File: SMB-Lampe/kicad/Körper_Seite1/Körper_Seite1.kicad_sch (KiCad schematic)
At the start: 24 parts, among them J10 Conn_01x01_Pin, J11 Conn_01x01_Pin, J12 Conn_01x01_Pin, J7 Conn_01x01_Pin, J8 Conn_01x01_Pin, J9 Conn_01x01_Pin

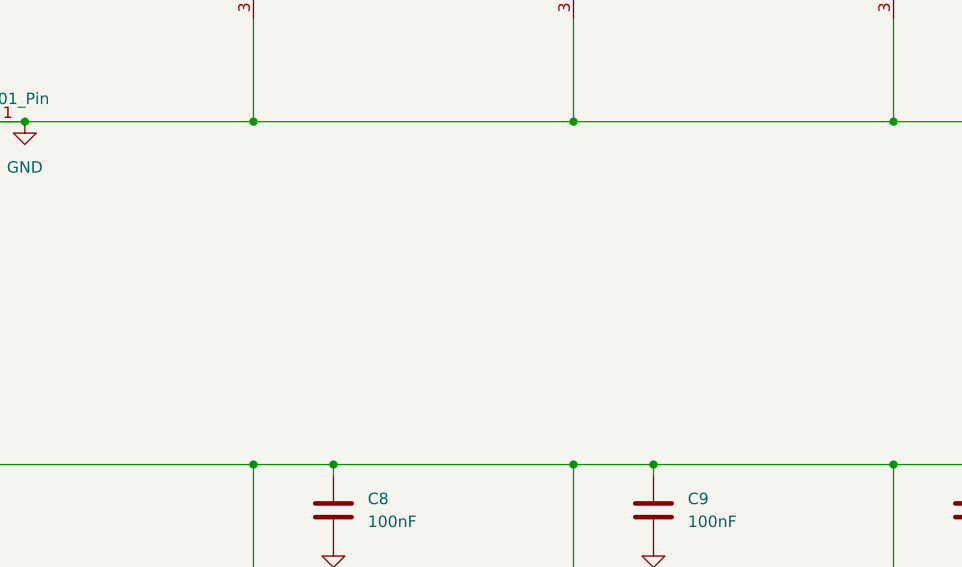
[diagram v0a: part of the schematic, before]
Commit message: Alle Platinen erstellt
Alle Platinen wurden im Projekt einzeln erstellt.
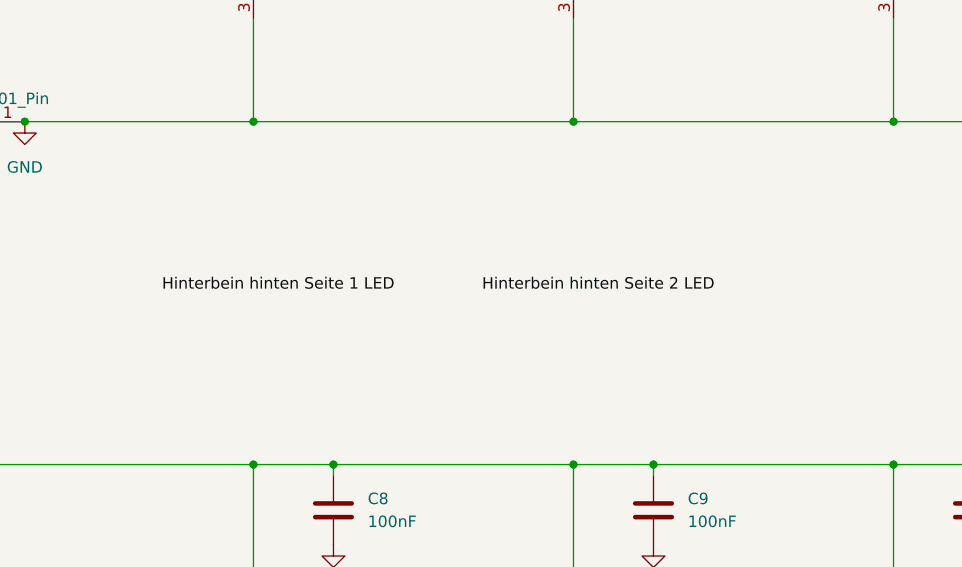
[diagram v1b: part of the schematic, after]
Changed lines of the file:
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@@
+		)
+	)
+	(label "Hinterbein hinten Seite 2 LED"
+		(at 88.9 82.55 0)
+		(effects
+			(font
+				(size 1.27 1.27)
+			)
+			(justify left bottom)
+		)
+	)
+	(label "Hinterbein hinten Seite 1 LED"
+		(at 53.34 82.55 0)
+		(effects
+			(font
+				(size 1.27 1.27)
+			)
+			(justify left bottom)
 		)
 	)

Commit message: Alle LEDs nochmal richtig angeschlossen
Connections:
- net Data: now also D7.2 (DOUT), D8.4 (DIN); no longer D7.4 (DIN), D8.2 (DOUT)
- net Data_In: now also D3.4 (DIN); no longer D3.2 (DOUT)
- net Data_OUT: now also D11.2 (DOUT); no longer D11.4 (DIN)
- net GND: no longer C10.1, C11.1, C3.1, C4.1, C5.1, C6.1, C7.1, C8.1, C9.1, D10.1 (VDD), D11.1 (VDD), D3.1 (VDD), D4.1 (VDD), D5.1 (VDD), D6.1 (VDD), D7.1 (VDD), D8.1 (VDD), D9.1 (VDD), J10.1 (Pin_1), J7.1 (Pin_1)
- net at D9.2 (DOUT): now also D10.4 (DIN); no longer D8.4 (DIN)
- net at D9.4 (DIN): now also D8.2 (DOUT); no longer D10.2 (DOUT)
- net at D6.2 (DOUT): now also D7.4 (DIN); no longer D5.4 (DIN)
- net at D6.4 (DIN): now also D5.2 (DOUT); no longer D7.2 (DOUT)
- net at D4.2 (DOUT): now also D5.4 (DIN); no longer D3.4 (DIN)
- net at D4.4 (DIN): now also D3.2 (DOUT); no longer D5.2 (DOUT)
- new net: D10.2 (DOUT), D11.4 (DIN)
- new net +5V: C10.1, C11.1, C3.1, C4.1, C5.1, C6.1, C7.1, C8.1, C9.1, D10.1 (VDD), D11.1 (VDD), D3.1 (VDD), D4.1 (VDD), D5.1 (VDD), D6.1 (VDD), D7.1 (VDD), D8.1 (VDD), D9.1 (VDD), J10.1 (Pin_1), J7.1 (Pin_1)
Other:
- moved on the sheet: C10, C11, C3, C4, C5, C6, C7, C8, C9

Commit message: Hinterbein Seite 1/2 erstellt
Anschlüsse zwischen den Platinen mit MountingHoles. Eigenes MountingHole Erstellt
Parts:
- J10, J11, J12, J7, J8, J9: footprint TestPoint:TestPoint_Pad_1.0x1.0mm -> TestPoint:TestPoint_Pad_2.0x2.0mm
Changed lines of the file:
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@@
 			)
 		)
-		(property "Footprint" "TestPoint:TestPoint_Pad_1.0x1.0mm"
+		(property "Footprint" "TestPoint:TestPoint_Pad_2.0x2.0mm"
 			(at 33.02 44.45 0)
 			(effects
@@
 			)
 		)
-		(property "Footprint" "TestPoint:TestPoint_Pad_1.0x1.0mm"
+		(property "Footprint" "TestPoint:TestPoint_Pad_2.0x2.0mm"
 			(at 33.02 25.4 0)
 			(effects
@@
 			)
 		)
-		(property "Footprint" "TestPoint:TestPoint_Pad_1.0x1.0mm"
+		(property "Footprint" "TestPoint:TestPoint_Pad_2.0x2.0mm"
 			(at 33.02 63.5 0)
 			(effects
@@
 			)
 		)
-		(property "Footprint" "TestPoint:TestPoint_Pad_1.0x1.0mm"
+		(property "Footprint" "TestPoint:TestPoint_Pad_2.0x2.0mm"
 			(at 259.08 101.6 0)
 			(effects
@@
 			)
 		)
-		(property "Footprint" "TestPoint:TestPoint_Pad_1.0x1.0mm"
+		(property "Footprint" "TestPoint:TestPoint_Pad_2.0x2.0mm"
 			(at 259.08 139.7 0)
 			(effects
@@
 			)
 		)
-		(property "Footprint" "TestPoint:TestPoint_Pad_1.0x1.0mm"
+		(property "Footprint" "TestPoint:TestPoint_Pad_2.0x2.0mm"
 			(at 259.08 120.65 0)
 			(effects

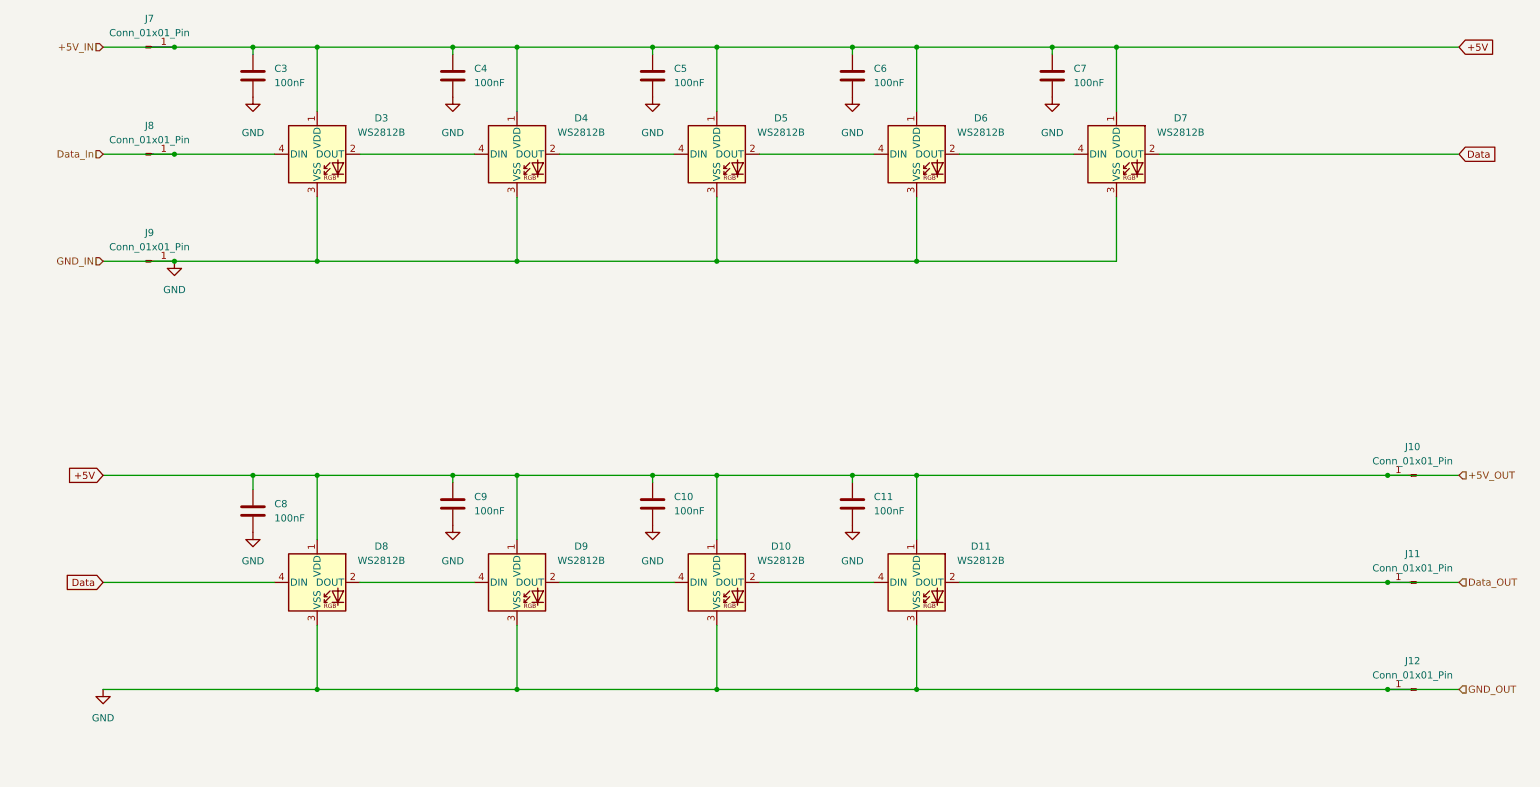
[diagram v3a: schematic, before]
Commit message: Vorderseite Platine Körper Seite 1 fertig
zwei GND Verbindungen fehlen noch
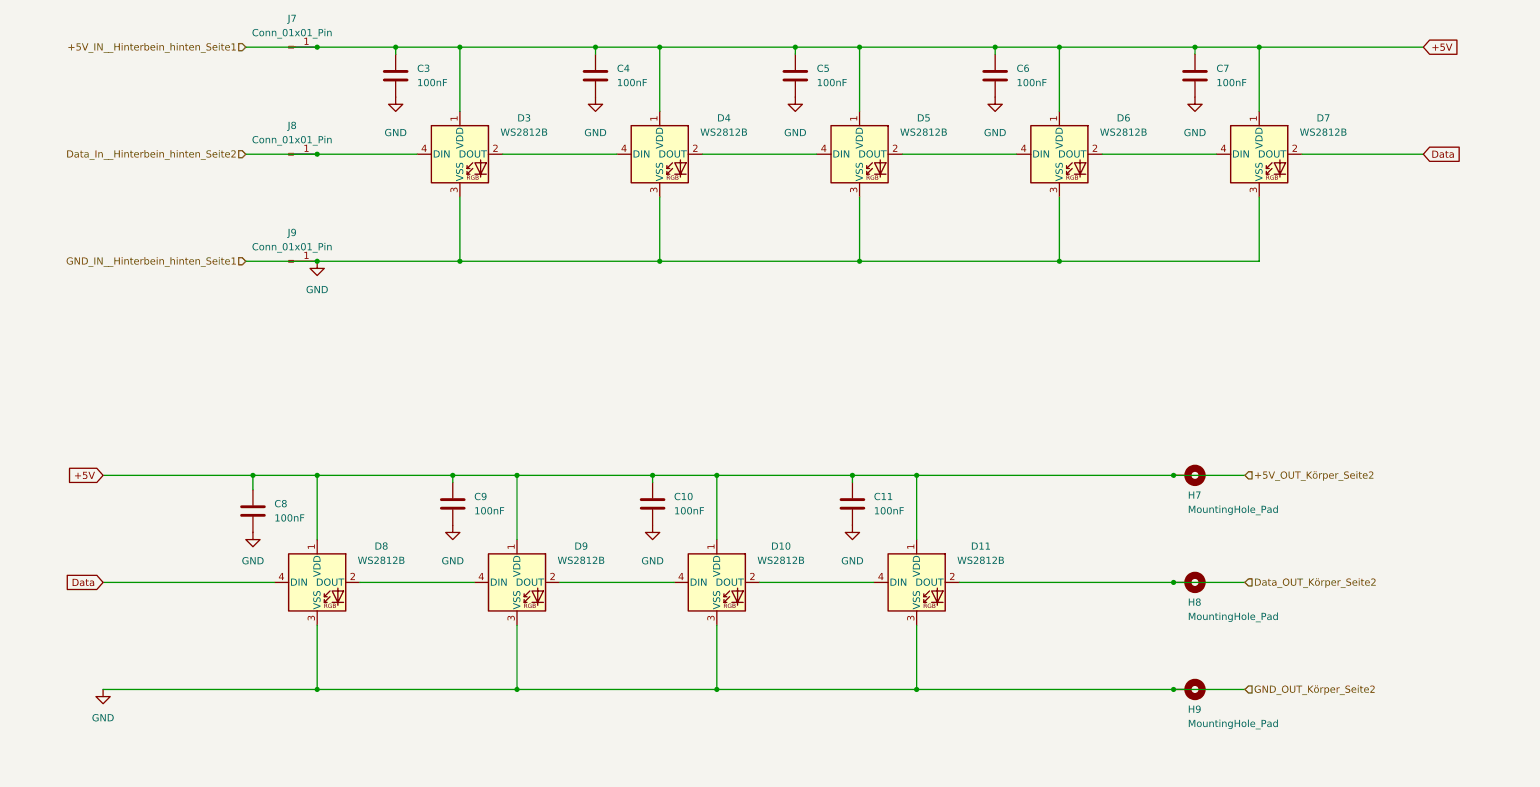
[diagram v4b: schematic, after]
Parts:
- removed J10, J11, J12: Conn_01x01_Pin, TestPoint:TestPoint_Pad_2.0x2.0mm, symbol Connector:Conn_01x01_Pin
- added H7, H8, H9: MountingHole_Pad, Eigenen_Library:MountingHole D2 x d1 test, symbol Mechanical:MountingHole_Pad
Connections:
- net +5V: now also H7.1
- net GND: now also H9.1
- net Data_In renamed Data_In__Hinterbein_hinten_Seite2
- net Data_OUT renamed Data_OUT_Körper_Seite2
- net Data_OUT_Körper_Seite2: now also H8.1
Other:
- moved on the sheet: C3, C4, C5, C6, C7, D3, D4, D5, D6, D7, J7, J8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

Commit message: Körper mit Vorder und Rückseite fertig
Alle Leiterbahnen sind gelegt und Verbindungen zu den anderen Platinen platziert
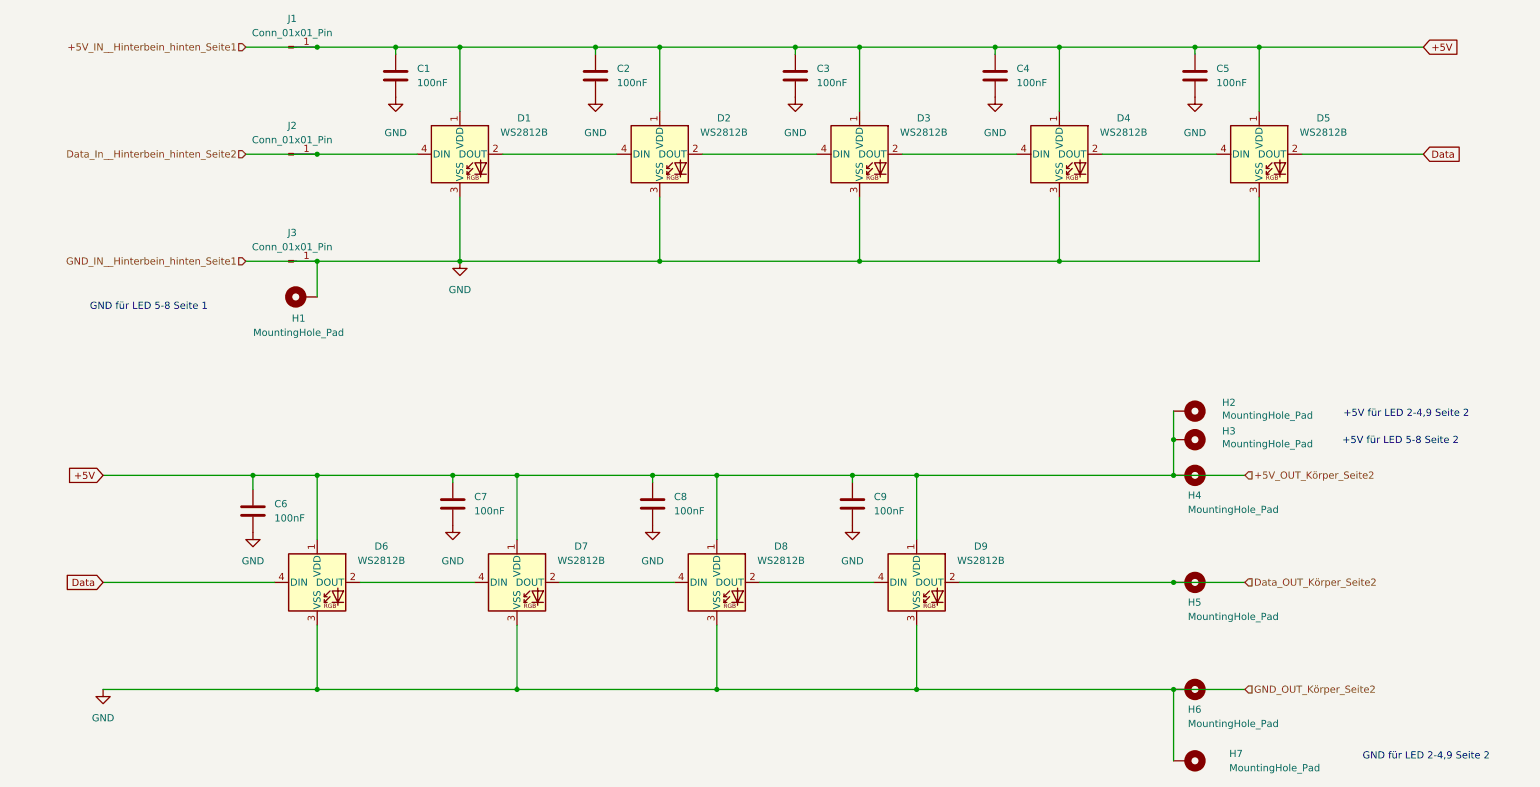
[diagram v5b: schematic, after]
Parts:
- added H1, H2, H3, H7: MountingHole_Pad, Eigenen_Library:MountingHole D2 x d1 test, symbol Mechanical:MountingHole_Pad
- renumbered C3 to C1, C4 to C2, C5 to C3, C6 to C4, C7 to C5, C8 to C6, C9 to C7, C10 to C8, C11 to C9, D3 to D1, D4 to D2, D5 to D3, D6 to D4, D7 to D5, D8 to D6, D9 to D7, D10 to D8, D11 to D9, H7 to H4, H8 to H5, H9 to H6, J7 to J1, J8 to J2, J9 to J3
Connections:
- net +5V: now also H2.1, H3.1
- net GND: now also H1.1, H7.1
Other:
- note added: "+5V für LED 2-4,9 Seite 2"
- note added: "+5V für LED 5-8 Seite 2"
- note added: "GND für LED 2-4,9 Seite 2"
- note added: "GND für LED 5-8 Seite 1"

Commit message: Vorderes Hinterbein fertig
Alle Platinen sind fertig beschaltet
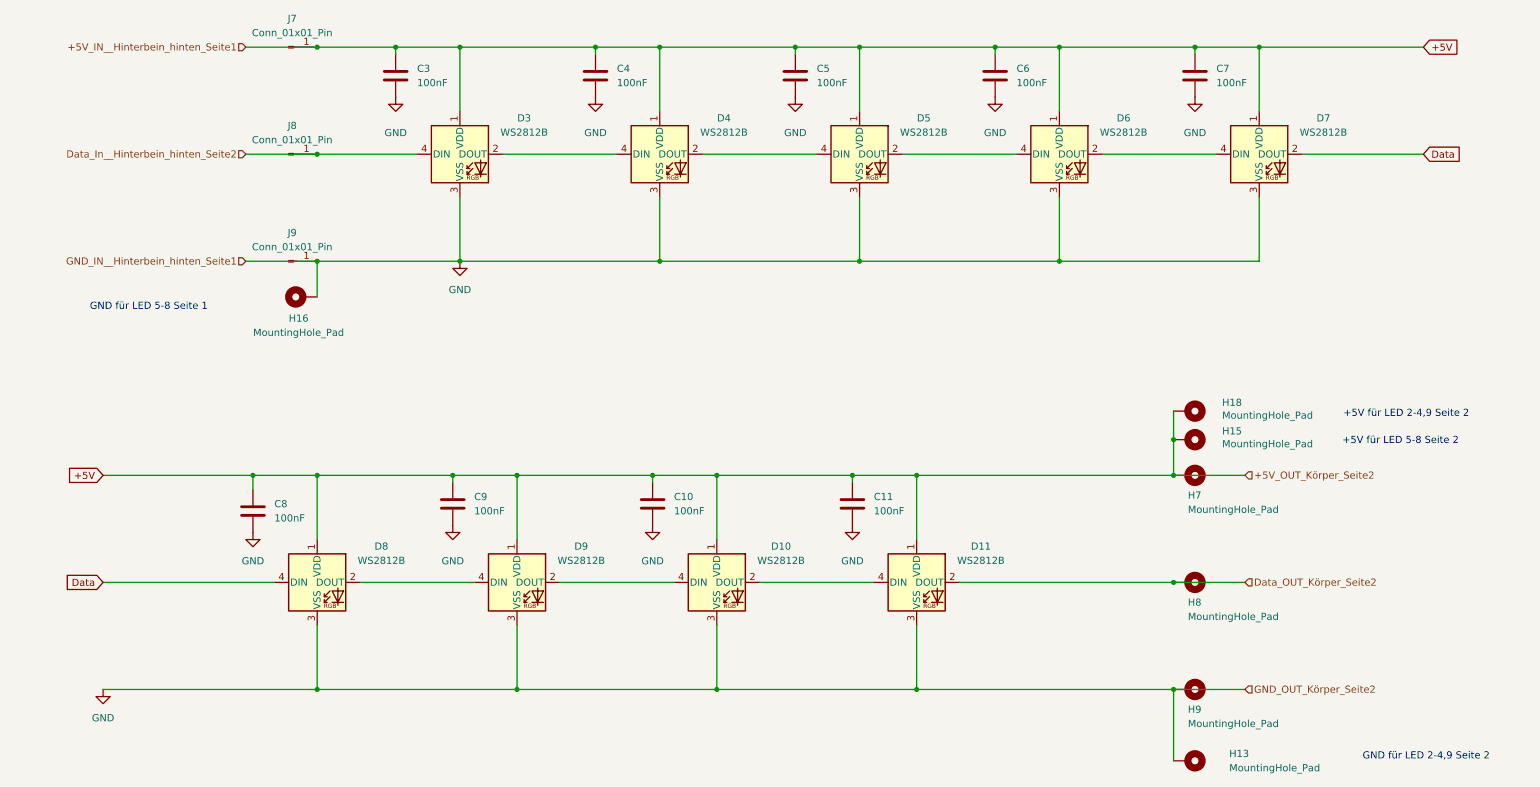
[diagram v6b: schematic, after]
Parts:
- renumbered C8 to C10, C9 to C11, C1 to C3, C2 to C4, C3 to C5, C4 to C6, C5 to C7, C6 to C8, C7 to C9, D8 to D10, D9 to D11, D1 to D3, D2 to D4, D3 to D5, D4 to D6, D5 to D7, D6 to D8, D7 to D9, H7 to H13, H3 to H15, H1 to H16, H2 to H18, H4 to H7, H5 to H8, H6 to H9, J1 to J7, J2 to J8, J3 to J9

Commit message: Hinterbeine Geändert teilweiße Körper
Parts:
- C10, C11, C3, C4, C5, C6, C7, C8, C9: footprint Capacitor_SMD:C_0201_0603Metric -> Capacitor_SMD:C_0603_1608Metric_Pad1.08x0.95mm_HandSolder
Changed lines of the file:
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@@
 			)
 		)
-		(property "Footprint" "Capacitor_SMD:C_0201_0603Metric"
+		(property "Footprint" "Capacitor_SMD:C_0603_1608Metric_Pad1.08x0.95mm_HandSolder"
 			(at 159.7152 110.49 0)
 			(effects
@@
 			)
 		)
-		(property "Footprint" "Capacitor_SMD:C_0201_0603Metric"
+		(property "Footprint" "Capacitor_SMD:C_0603_1608Metric_Pad1.08x0.95mm_HandSolder"
 			(at 78.4352 34.29 0)
 			(effects
@@
 			)
 		)
-		(property "Footprint" "Capacitor_SMD:C_0201_0603Metric"
+		(property "Footprint" "Capacitor_SMD:C_0603_1608Metric_Pad1.08x0.95mm_HandSolder"
 			(at 149.5552 34.29 0)
 			(effects
@@
 			)
 		)
-		(property "Footprint" "Capacitor_SMD:C_0201_0603Metric"
+		(property "Footprint" "Capacitor_SMD:C_0603_1608Metric_Pad1.08x0.95mm_HandSolder"
 			(at 220.6752 34.29 0)
 			(effects
@@
 			)
 		)
-		(property "Footprint" "Capacitor_SMD:C_0201_0603Metric"
+		(property "Footprint" "Capacitor_SMD:C_0603_1608Metric_Pad1.08x0.95mm_HandSolder"
 			(at 88.5952 110.49 0)
 			(effects
@@
 			)
 		)
-		(property "Footprint" "Capacitor_SMD:C_0201_0603Metric"
+		(property "Footprint" "Capacitor_SMD:C_0603_1608Metric_Pad1.08x0.95mm_HandSolder"
 			(at 53.0352 111.76 0)
 			(effects
@@
 			)
 		)
-		(property "Footprint" "Capacitor_SMD:C_0201_0603Metric"
+		(property "Footprint" "Capacitor_SMD:C_0603_1608Metric_Pad1.08x0.95mm_HandSolder"
 			(at 185.1152 34.29 0)
 			(effects
@@
 			)
 		)
-		(property "Footprint" "Capacitor_SMD:C_0201_0603Metric"
+		(property "Footprint" "Capacitor_SMD:C_0603_1608Metric_Pad1.08x0.95mm_HandSolder"
 			(at 113.9952 34.29 0)
 			(effects
@@
 			)
 		)
-		(property "Footprint" "Capacitor_SMD:C_0201_0603Metric"
+		(property "Footprint" "Capacitor_SMD:C_0603_1608Metric_Pad1.08x0.95mm_HandSolder"
 			(at 124.1552 110.49 0)
 			(effects

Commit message: Nachträgliche Änderungen für die Fertigung und Präsentation
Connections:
- net +5V renamed +5V_1
- net Data renamed Data1
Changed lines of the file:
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@@
 		)
 	)
-	(global_label "Data"
+	(global_label "Data1"
 		(shape input)
 		(at 25.4 120.65 180)
@@
 		)
 		(property "Intersheetrefs" "${INTERSHEET_REFS}"
-			(at 18.1211 120.65 0)
+			(at 16.9116 120.65 0)
 			(effects
 				(font
@@
 		)
 	)
-	(global_label "+5V"
+	(global_label "+5V_1"
 		(shape input)
 		(at 25.4 101.6 180)
@@
 		)
 		(property "Intersheetrefs" "${INTERSHEET_REFS}"
-			(at 18.5443 101.6 0)
+			(at 16.3672 101.6 0)
 			(effects
 				(font
@@
 		)
 	)
-	(global_label "+5V"
+	(global_label "+5V_1"
 		(shape input)
 		(at 260.35 25.4 0)
@@
 		)
 		(property "Intersheetrefs" "${INTERSHEET_REFS}"
-			(at 267.2057 25.4 0)
+			(at 269.3828 25.4 0)
 			(effects
 				(font
@@
 		)
 	)
-	(global_label "Data"
+	(global_label "Data1"
 		(shape input)
 		(at 260.35 44.45 0)
@@
 		)
 		(property "Intersheetrefs" "${INTERSHEET_REFS}"
-			(at 267.6289 44.45 0)
+			(at 268.8384 44.45 0)
 			(effects
 				(font
